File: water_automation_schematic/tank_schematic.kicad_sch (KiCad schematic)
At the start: 3 parts, among them SW1 SW_DPST_x2, SW2 SW_DPST_x2, U1 lolin32_lite_V1.00

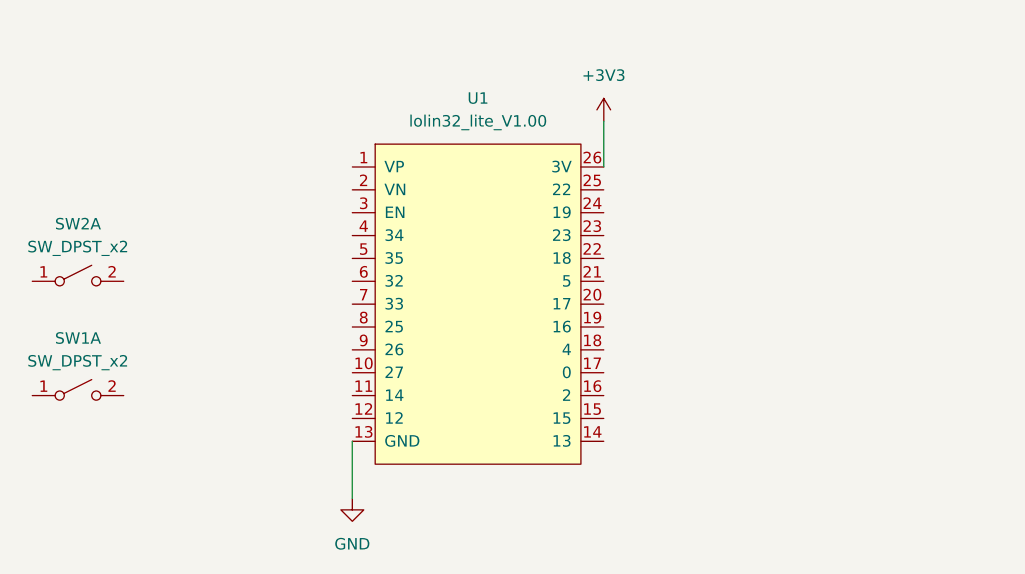
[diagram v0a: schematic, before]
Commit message: added us sensor logic
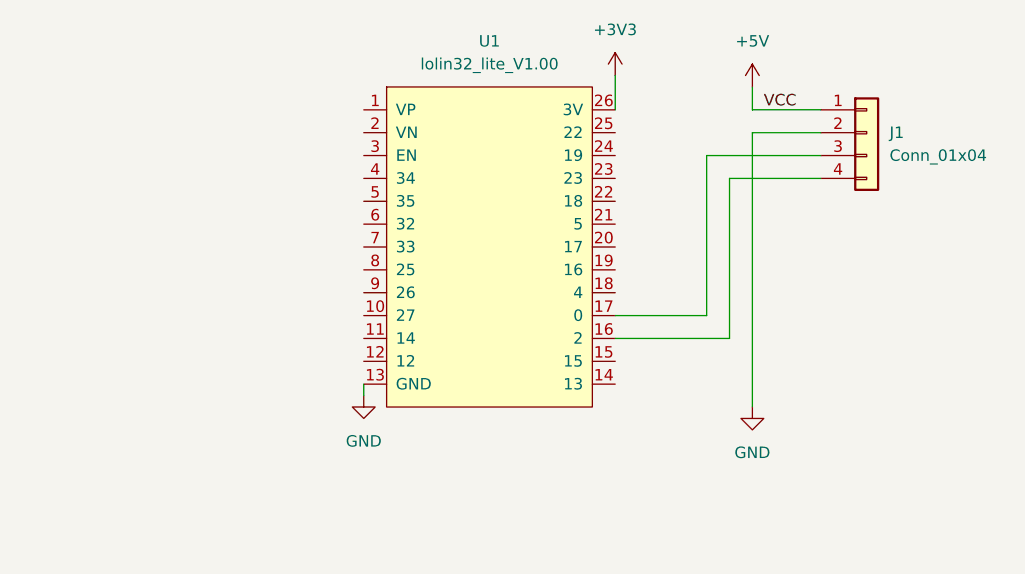
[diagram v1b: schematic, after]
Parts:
- removed SW1, SW2: SW_DPST_x2, symbol Switch:SW_DPST_x2
- added J1: Conn_01x04, symbol Connector_Generic:Conn_01x04
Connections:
- net GND: now also J1.2 (Pin_2)
- net at U1.16 (2): now also J1.4 (Pin_4)
- net at U1.17 (0): now also J1.3 (Pin_3)
- new net +5V: J1.1 (Pin_1)
